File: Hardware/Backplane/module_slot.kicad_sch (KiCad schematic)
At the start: 40 parts, among them J201 Conn_01x10, J202 10018784-10201TLF, J203 Conn_01x06, Q201 NMOS, Q202 PMOS, Q203 PMOS, Q204 PMOS

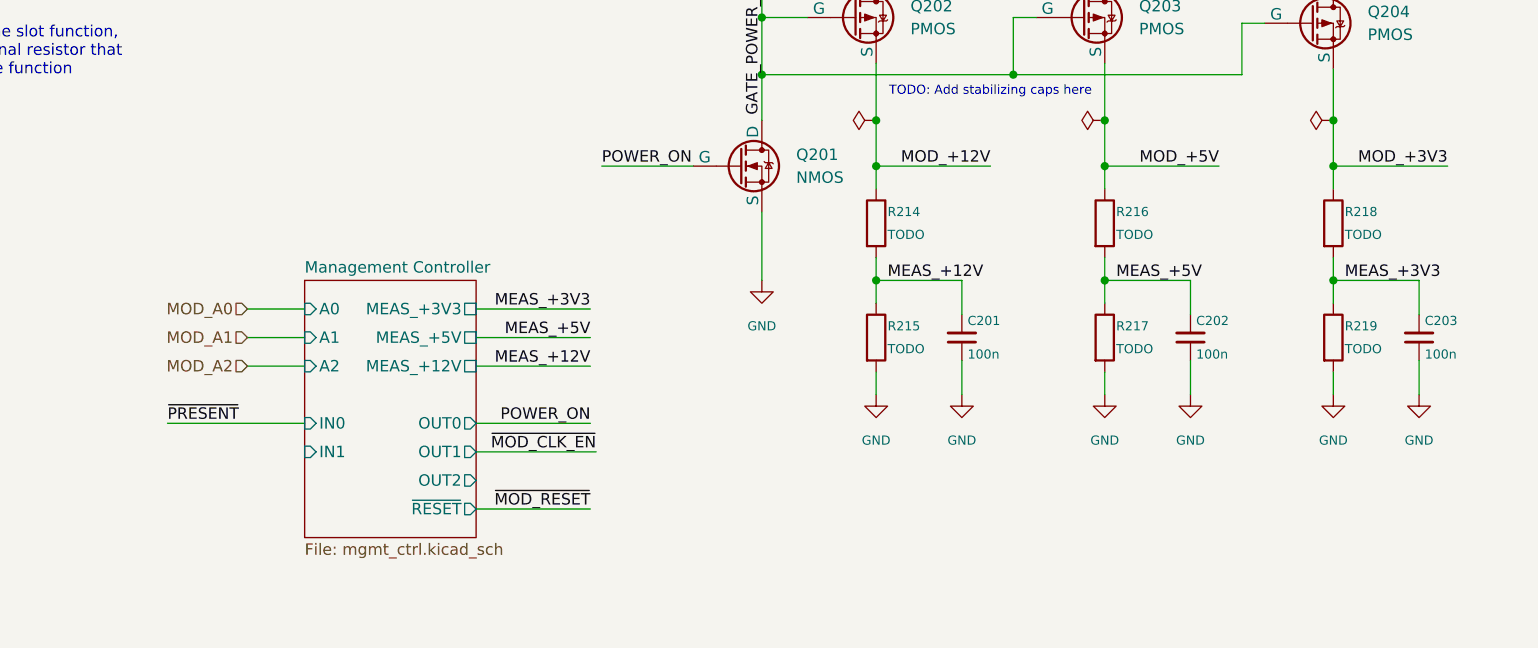
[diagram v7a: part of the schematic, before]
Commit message: Updates backplane: Improves voltage measurement dividers, replaces DS1307+ RTC with a much cheaper one, replaces 8 MHz global clock with 48 MHz global clock
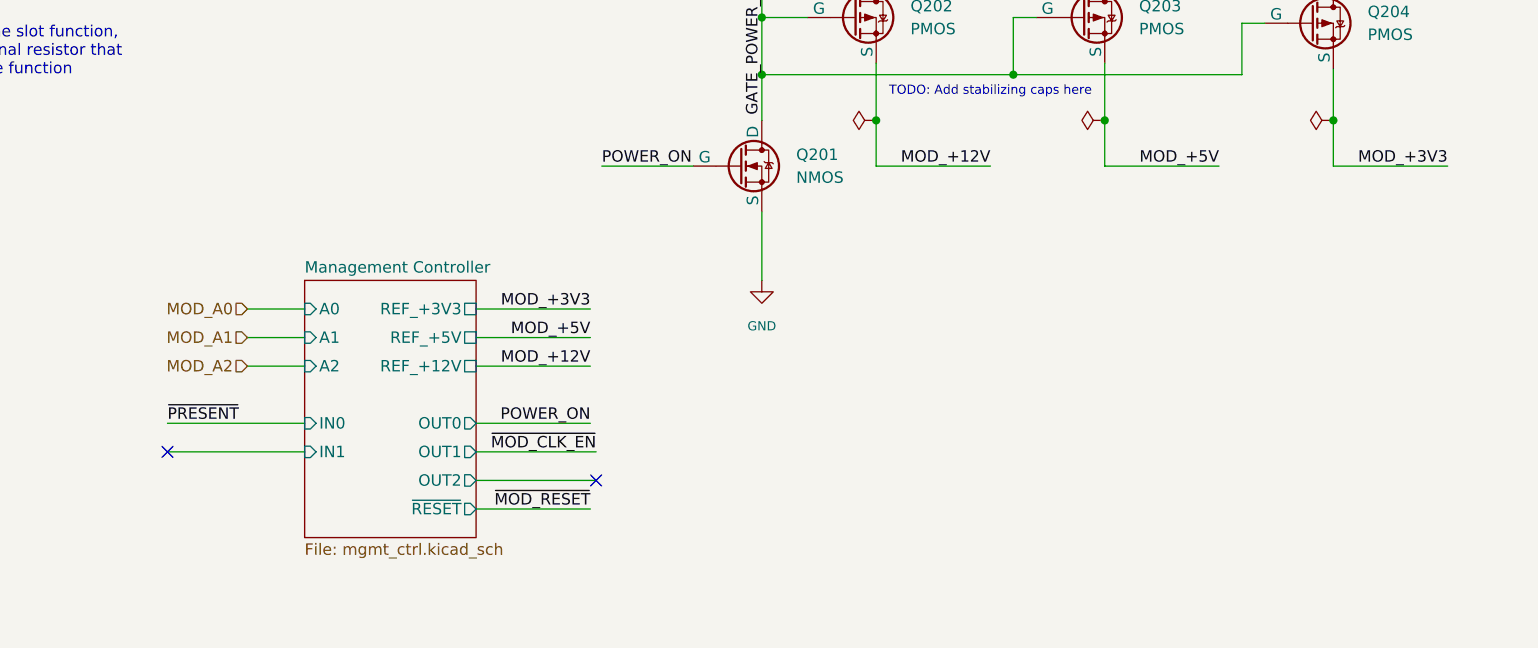
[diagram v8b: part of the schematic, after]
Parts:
- removed C201, C202, C203: 100n, Capacitor_SMD:C_0603_1608Metric, symbol Device:C_Small
- removed R214, R215, R216, R217, R218, R219: TODO, Resistor_SMD:R_0603_1608Metric, symbol Device:R
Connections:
- no-connect marks 8 -> 10
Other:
- sheet Management Controller ports: added REF_+12V, REF_+3V3, REF_+5V; removed MEAS_+12V, MEAS_+3V3, MEAS_+5V
